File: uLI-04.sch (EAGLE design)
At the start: 39 parts, among them IC1 PIC18F14K50-I/SS, IC2 ADM2483, IC3 MCP130T, IC4 78L05F, J1 PICPROG2-V, J5 WEBP6-4, J6 WEBP6-4, J7 WEBP6-4, Q1 12.00 MHz, T1 IRF7306, X1 MINI-USB_SHIELD4P-USB-SPEC, X2 ARK1550/2_S

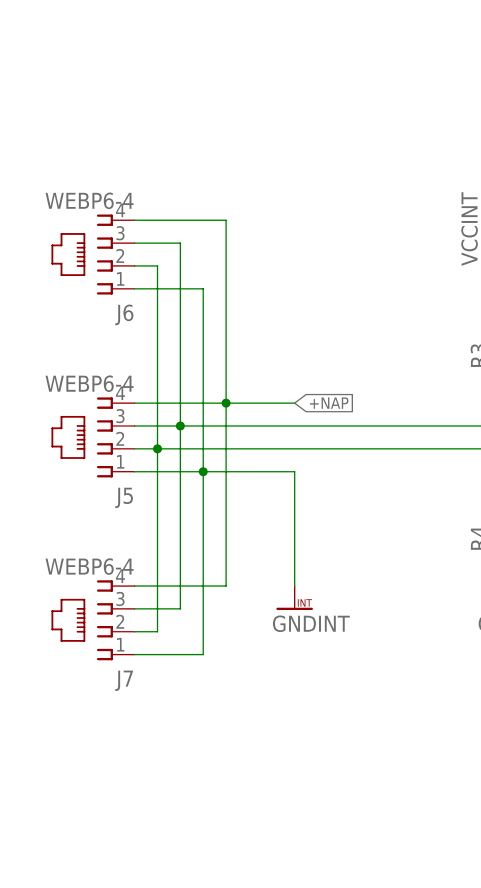
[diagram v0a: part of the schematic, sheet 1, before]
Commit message: 6-4 > 6-6, ploska J5.
 * Konektory WEBP 6-4 nahrazeny za WEBP 6-6. Close #3.
 * Pajeci ploska pobliz J5 odstranena. Close 2.
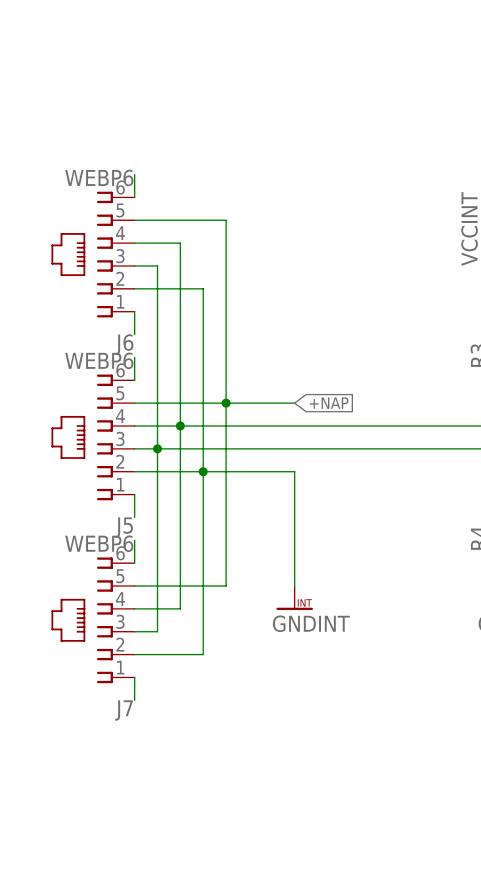
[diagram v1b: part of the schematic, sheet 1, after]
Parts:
- J5, J6, J7: value WEBP6-4 -> WEBP6; device con-malina:WEBP6-4_SHORT -> con-malina:WEBP6-6_SPEC2
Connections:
- new net N$11: J6.1
- new net N$12: J5.6
- new net N$13: J5.1
- new net N$14: J7.6
- new net N$15: J7.1
- new net N$8: J6.6
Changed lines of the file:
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@@
 <part name="T1" library="transistor-fet" deviceset="IRF7306" device=""/>
 <part name="C10" library="rcl" deviceset="CPOL-EU" device="E2-5" value="22u/25V"/>
-<part name="J5" library="con-malina" deviceset="WEBP6-4" device="_SHORT" value="WEBP6-4">
+<part name="J5" library="con-malina" deviceset="WEBP6-6" device="_SPEC2" value="WEBP6">
 <variant name="slave" populate="no"/>
 </part>
-<part name="J6" library="con-malina" deviceset="WEBP6-4" device="_SHORT" value="WEBP6-4">
+<part name="J6" library="con-malina" deviceset="WEBP6-6" device="_SPEC2" value="WEBP6">
 <variant name="slave" populate="no"/>
 </part>
-<part name="J7" library="con-malina" deviceset="WEBP6-4" device="_SHORT" value="WEBP6-4">
+<part name="J7" library="con-malina" deviceset="WEBP6-6" device="_SPEC2" value="WEBP6">
 <variant name="master" populate="no"/>
 </part>
@@
 </segment>
 </net>
+<net name="N$8" class="1">
+<segment>
+<pinref part="J6" gate="A" pin="6"/>
+<wire x1="25.4" y1="106.68" x2="25.4" y2="109.22" width="0.1524" layer="91"/>
+</segment>
+</net>
+<net name="N$11" class="1">
+<segment>
+<pinref part="J6" gate="A" pin="1"/>
+<wire x1="25.4" y1="93.98" x2="25.4" y2="91.44" width="0.1524" layer="91"/>
+</segment>
+</net>
+<net name="N$12" class="1">
+<segment>
+<pinref part="J5" gate="A" pin="6"/>
+<wire x1="25.4" y1="86.36" x2="25.4" y2="88.9" width="0.1524" layer="91"/>
+</segment>
+</net>
+<net name="N$13" class="1">
+<segment>
+<pinref part="J5" gate="A" pin="1"/>
+<wire x1="25.4" y1="73.66" x2="25.4" y2="71.12" width="0.1524" layer="91"/>
+</segment>
+</net>
+<net name="N$14" class="1">
+<segment>
+<pinref part="J7" gate="A" pin="6"/>
+<wire x1="25.4" y1="66.04" x2="25.4" y2="68.58" width="0.1524" layer="91"/>
+</segment>
+</net>
+<net name="N$15" class="1">
+<segment>
+<pinref part="J7" gate="A" pin="1"/>
+<wire x1="25.4" y1="53.34" x2="25.4" y2="50.8" width="0.1524" layer="91"/>
+</segment>
+</net>

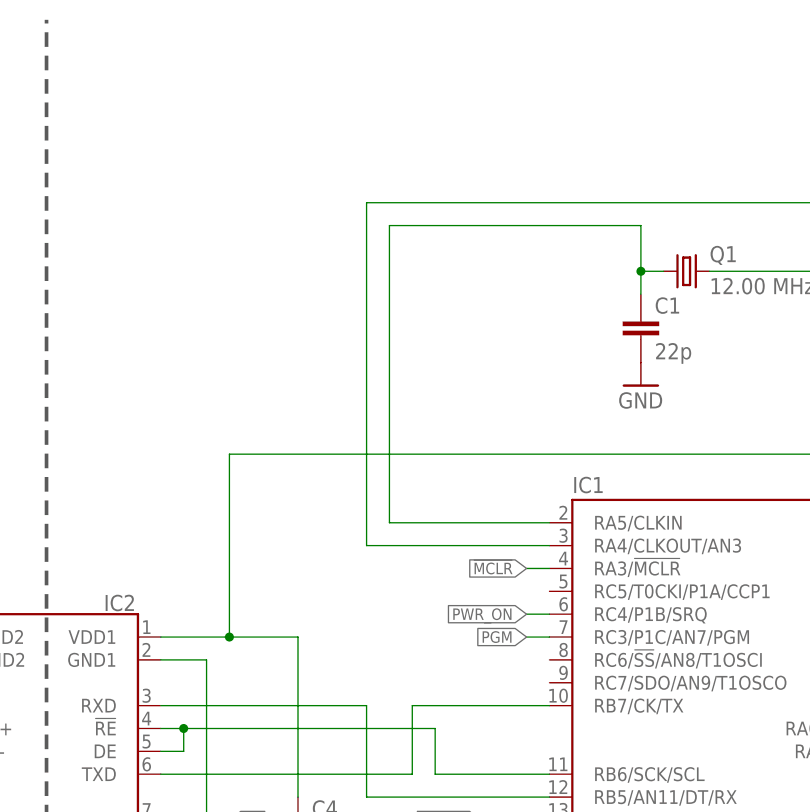
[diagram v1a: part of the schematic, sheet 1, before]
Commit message: Doplnen rezistor 10k na pin PGM (#9).
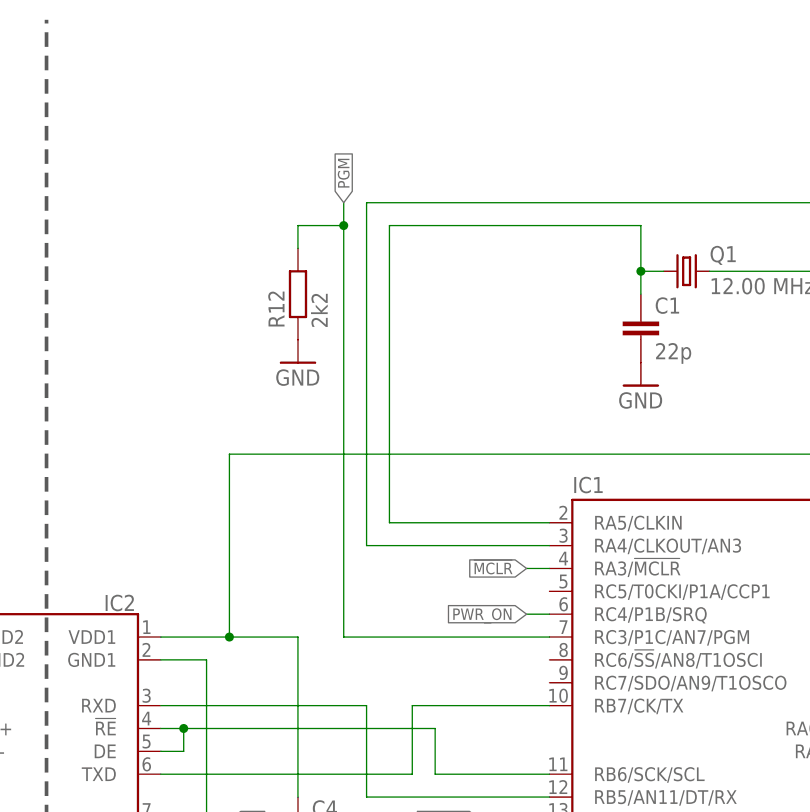
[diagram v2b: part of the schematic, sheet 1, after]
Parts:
- added R12: 2k2, rcl:R-EU_R1206
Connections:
- net GND: now also R12.1
- net PGM: now also R12.2
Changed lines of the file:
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@@
 <part name="GND14" library="supply1" deviceset="GND" device=""/>
 <part name="IC3" library="my" deviceset="MCP130T" device=""/>
+<part name="R12" library="rcl" deviceset="R-EU_" device="R1206" value="2k2"/>
+<part name="GND15" library="supply1" deviceset="GND" device=""/>
 </parts>
 <sheets>
@@
 <instance part="J6" gate="A" x="22.86" y="99.06" rot="R180"/>
 <instance part="J7" gate="A" x="22.86" y="58.42" rot="R180"/>
+<instance part="R12" gate="G$1" x="147.32" y="134.62" rot="R90"/>
+<instance part="GND15" gate="1" x="147.32" y="127"/>
 </instances>
 <busses>
@@
 <pinref part="GND9" gate="1" pin="GND"/>
 <wire x1="165.1" y1="35.56" x2="165.1" y2="40.64" width="0.1524" layer="91"/>
+</segment>
+<segment>
+<pinref part="R12" gate="G$1" pin="1"/>
+<pinref part="GND15" gate="1" pin="GND"/>
 </segment>
 </net>
@@
 <segment>
 <pinref part="IC1" gate="A" pin="RC3/P1C/AN7/PGM"/>
-<wire x1="175.26" y1="96.52" x2="172.72" y2="96.52" width="0.1524" layer="91"/>
-<label x="172.72" y="96.52" size="1.27" layer="95" font="vector" ratio="12" rot="MR0" xref="yes"/>
-</segment>
-</net>
+<label x="152.4" y="144.78" size="1.27" layer="95" font="vector" ratio="12" rot="MR90" xref="yes"/>
+<wire x1="175.26" y1="96.52" x2="152.4" y2="96.52" width="0.1524" layer="91"/>
+<wire x1="152.4" y1="96.52" x2="152.4" y2="142.24" width="0.1524" layer="91"/>
+<pinref part="R12" gate="G$1" pin="2"/>
+<wire x1="152.4" y1="142.24" x2="152.4" y2="144.78" width="0.1524" layer="91"/>
+<wire x1="152.4" y1="142.24" x2="147.32" y2="142.24" width="0.1524" layer="91"/>
+<wire x1="147.32" y1="142.24" x2="147.32" y2="139.7" width="0.1524" layer="91"/>
+<junction x="152.4" y="142.24"/>
+</segment>
+</net>
